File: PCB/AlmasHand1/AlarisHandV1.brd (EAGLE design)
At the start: 96.5 x 68.2 mm, 13 parts, among them M1 22-23-2021, M2 22-23-2021, M3 22-23-2021, M4 22-23-2021, M5 22-23-2021, M6 22-23-2021

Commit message: updates on board
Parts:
- moved U$1 2.54 mm to (25.4, 14.0)
- moved M1 2.54 mm to (10.2, 15.2)
- moved M2 2.54 mm to (10.2, 20.3)
- moved MOTOR_POWER_CONNECTOR 2.54 mm to (10.2, 27.9)
- moved UART 2.54 mm to (10.2, 38.1)
- moved U$2 1.27 mm to (66.0, 21.6)
- moved U$3 1.27 mm to (66.0, 48.3)
- moved M3 1.27 mm to (82.5, 47.0)
- moved M4 1.27 mm to (82.5, 41.9)
- moved M5 1.27 mm to (81.3, 20.3)
- moved M6 1.27 mm to (81.3, 15.2)
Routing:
- net 3.3V: track 0.00 -> 173.6 mm
- net GND: track 0.00 -> 137.1 mm
- net MOTOR_POWER: track 0.00 -> 114.9 mm
- net N$25: track 0.00 -> 60.5 mm
- net N$32: track 0.00 -> 54.6 mm
- net UART_RX: track 0.00 -> 54.6 mm
- net UART_TX: track 0.00 -> 53.7 mm
- net N$26: track 0.00 -> 48.9 mm
- net N$7: track 0.00 -> 45.2 mm
- net N$8: track 0.00 -> 37.9 mm
- net N$31: track 0.00 -> 36.4 mm
- net N$4: track 0.00 -> 21.7 mm
- net N$3: track 0.00 -> 21.5 mm
- net N$2: track 0.00 -> 15.1 mm
- net N$5: track 0.00 -> 12.0 mm
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
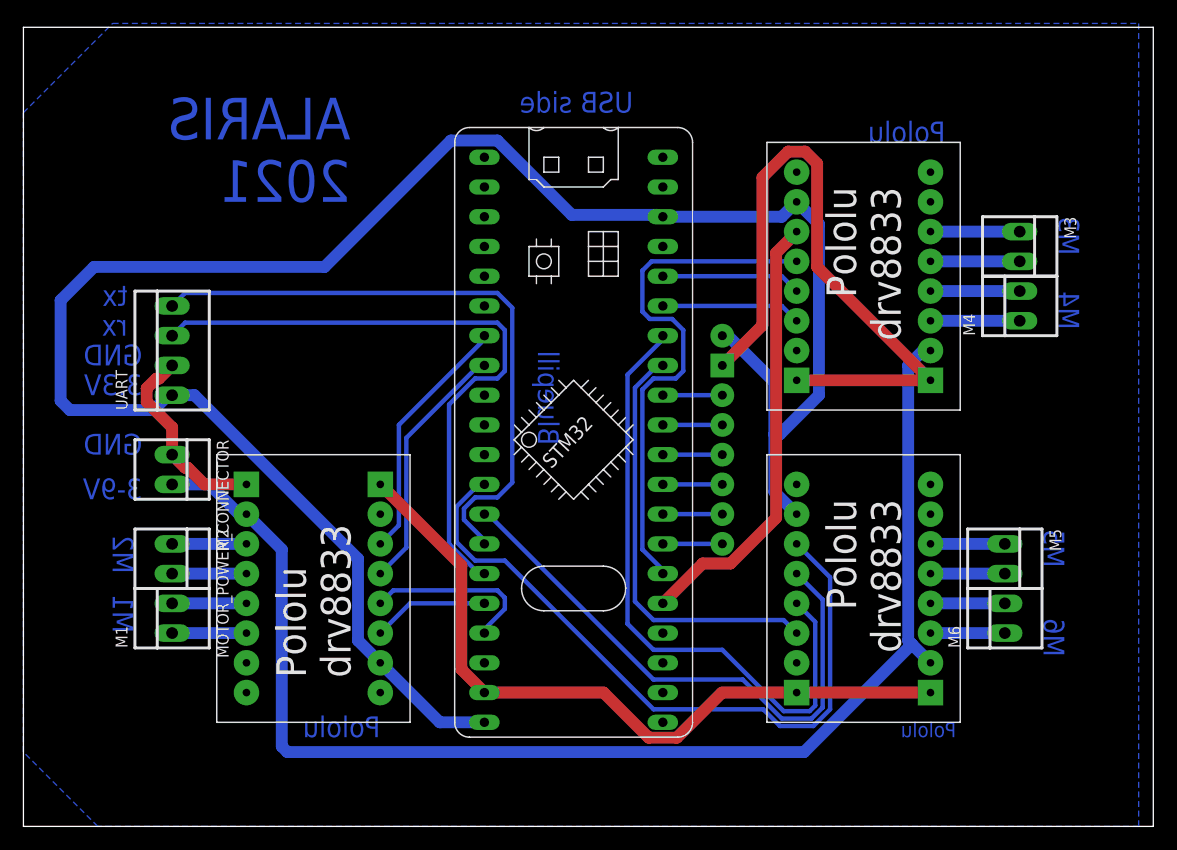
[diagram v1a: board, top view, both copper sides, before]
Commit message: Updated PCB drills for printing
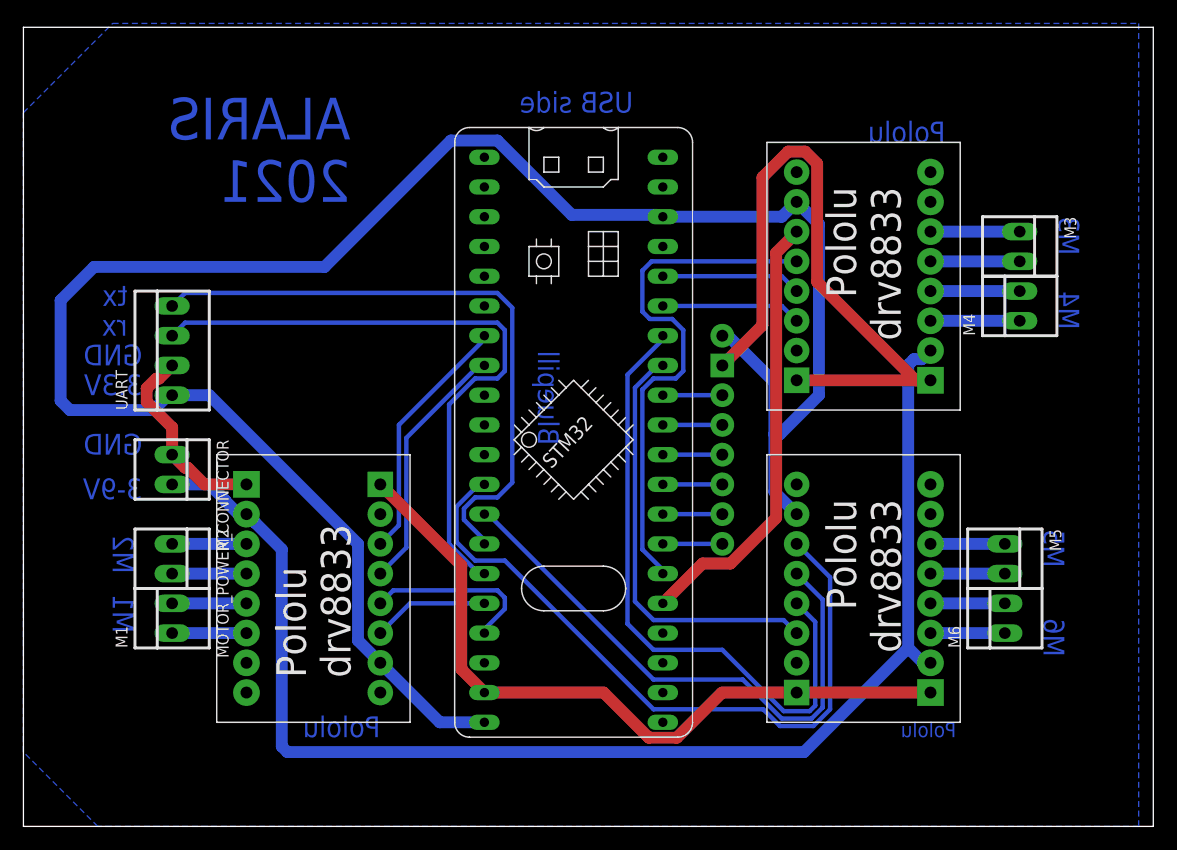
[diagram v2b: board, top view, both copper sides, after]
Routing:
- net GND: track 137.1 -> 137.9 mm
- net 3.3V: track 173.6 -> 174.3 mm
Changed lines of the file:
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@@
 <contactref element="MOTOR_POWER_CONNECTOR" pad="2"/>
 <wire x1="13.335" y1="26.67" x2="10.16" y2="26.67" width="1.016" layer="16"/>
-<wire x1="15.875" y1="24.13" x2="13.335" y2="26.67" width="1.016" layer="16"/>
-<wire x1="16.51" y1="24.13" x2="15.875" y2="24.13" width="1.016" layer="16"/>
-<wire x1="73.025" y1="13.335" x2="73.3425" y2="13.0175" width="1.016" layer="16"/>
-<wire x1="73.3425" y1="13.0175" x2="74.93" y2="11.43" width="1.016" layer="16"/>
-<wire x1="73.025" y1="36.83" x2="73.025" y2="13.335" width="1.016" layer="16"/>
-<wire x1="74.295" y1="38.1" x2="73.025" y2="36.83" width="1.016" layer="16"/>
-<wire x1="74.93" y1="38.1" x2="74.295" y2="38.1" width="1.016" layer="16"/>
-<wire x1="19.52625" y1="21.11375" x2="16.51" y2="24.13" width="1.016" layer="16"/>
-<wire x1="19.52625" y1="4.28625" x2="19.52625" y2="21.11375" width="1.016" layer="16"/>
 <wire x1="20.0025" y1="3.81" x2="19.52625" y2="4.28625" width="1.016" layer="16"/>
 <wire x1="64.135" y1="3.81" x2="20.0025" y2="3.81" width="1.016" layer="16"/>
-<wire x1="73.3425" y1="13.0175" x2="64.135" y2="3.81" width="1.016" layer="16"/>
+<wire x1="73.025" y1="12.7" x2="64.135" y2="3.81" width="1.016" layer="16"/>
+<wire x1="17.25699375" y1="23.3934" x2="17.2466" y2="23.3934" width="1.016" layer="16"/>
+<wire x1="17.2466" y1="23.3934" x2="16.51" y2="24.13" width="1.016" layer="16"/>
+<wire x1="19.52625" y1="4.28625" x2="19.52625" y2="21.12414375" width="1.016" layer="16"/>
+<wire x1="19.52625" y1="21.12414375" x2="17.25699375" y2="23.3934" width="1.016" layer="16"/>
+<wire x1="14.7066" y1="25.25345625" x2="14.7066" y2="25.2984" width="1.016" layer="16"/>
+<wire x1="14.7066" y1="25.2984" x2="13.335" y2="26.67" width="1.016" layer="16"/>
+<wire x1="16.51" y1="24.13" x2="15.83005625" y2="24.13" width="1.016" layer="16"/>
+<wire x1="15.83005625" y1="24.13" x2="14.7066" y2="25.25345625" width="1.016" layer="16"/>
+<wire x1="74.93" y1="38.1" x2="74.1934" y2="37.3634" width="1.016" layer="16"/>
+<wire x1="74.1934" y1="37.3634" x2="73.51345625" y2="37.3634" width="1.016" layer="16"/>
+<wire x1="73.51345625" y1="37.3634" x2="73.025" y2="36.87494375" width="1.016" layer="16"/>
+<wire x1="73.025" y1="36.87494375" x2="73.025" y2="12.7" width="1.016" layer="16"/>
+<wire x1="74.93" y1="11.43" x2="74.295" y2="11.43" width="1.016" layer="16"/>
+<wire x1="74.295" y1="11.43" x2="73.025" y2="12.7" width="1.016" layer="16"/>
 </signal>
 <signal name="N$16">
@@
 <wire x1="64.22595625" y1="55.0926" x2="62.77404375" y2="55.0926" width="1.016" layer="1"/>
 <wire x1="60.579" y1="40.259" x2="57.15" y2="36.83" width="1.016" layer="1"/>
-<wire x1="65.2526" y1="45.2374" x2="65.2526" y2="54.06595625" width="1.016" layer="1"/>
-<wire x1="74.93" y1="35.56" x2="65.2526" y2="45.2374" width="1.016" layer="1"/>
+<wire x1="65.2526" y1="43.9674" x2="65.2526" y2="54.06595625" width="1.016" layer="1"/>
+<wire x1="74.93" y1="35.56" x2="73.66" y2="35.56" width="1.016" layer="1"/>
+<wire x1="73.66" y1="35.56" x2="65.2526" y2="43.9674" width="1.016" layer="1"/>
 <wire x1="62.77404375" y1="55.0926" x2="60.579" y2="52.89755625" width="1.016" layer="1"/>
 <wire x1="60.579" y1="52.89755625" x2="60.579" y2="40.259" width="1.016" layer="1"/>
@@
 <wire x1="33.02" y1="6.35" x2="36.83" y2="6.35" width="1.016" layer="16"/>
 <wire x1="27.94" y1="11.43" x2="33.02" y2="6.35" width="1.016" layer="16"/>
-<wire x1="12.065" y1="34.29" x2="10.16" y2="34.29" width="1.016" layer="16"/>
-<wire x1="26.035" y1="20.32" x2="12.065" y2="34.29" width="1.016" layer="16"/>
-<wire x1="26.035" y1="13.335" x2="26.035" y2="20.32" width="1.016" layer="16"/>
+<wire x1="13.335" y1="34.29" x2="10.16" y2="34.29" width="1.016" layer="16"/>
+<wire x1="26.035" y1="21.59" x2="13.335" y2="34.29" width="1.016" layer="16"/>
+<wire x1="26.035" y1="13.335" x2="26.035" y2="21.59" width="1.016" layer="16"/>
 <wire x1="27.94" y1="11.43" x2="26.035" y2="13.335" width="1.016" layer="16"/>
 <wire x1="44.29125" y1="49.68875" x2="51.59375" y2="49.68875" width="1.016" layer="16"/>

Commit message: fixed M1 port connection
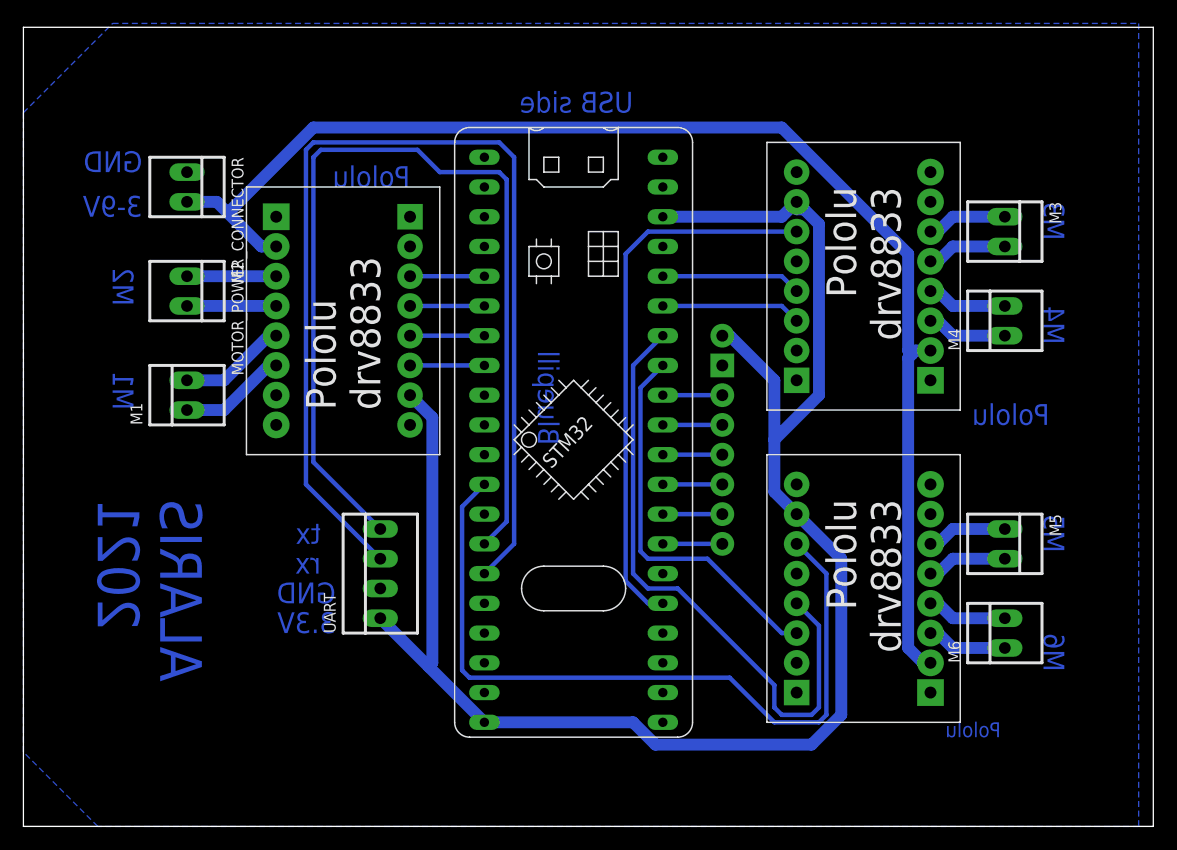
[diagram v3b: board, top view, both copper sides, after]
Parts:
- moved UART 26.1 mm to (27.9, 19.1)
- moved MOTOR_POWER_CONNECTOR 24.2 mm to (11.4, 52.1)
- moved U$1 23.0 mm to (27.9, 36.8)
- moved M2 22.9 mm to (11.4, 43.2)
- moved M1 19.1 mm to (11.4, 34.3)
- moved M3 1.80 mm to (81.3, 48.3)
- moved M4 1.80 mm to (81.3, 40.6)
- moved M5 1.27 mm to (81.3, 21.6)
- moved M6 1.27 mm to (81.3, 14.0)
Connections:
- net UART_TX renamed N$1
- removed net N$1 (its old number): U$1.INA1, U$4.P$16
- new net N$9: U$1.INB1, U$4.P$5
- net N$2: now also U$1.INA1, U$4.P$8; no longer U$1.INA2, U$4.P$17
- net N$3: now also U$1.INA2; no longer U$1.INB1
- net N$4: now also U$4.P$6; no longer U$4.P$8
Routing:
- net GND: track 137.9 -> 0.00 mm
- net N$26: track 48.9 -> 0.00 mm
- net N$7: track 45.2 -> 0.00 mm
- net UART_RX: track 54.6 -> 92.7 mm
- net 3.3V: track 174.3 -> 141.0 mm
- net N$1: track 53.7 -> 83.8 mm
- net N$4: track 21.7 -> 6.35 mm
- net N$3: track 21.5 -> 6.35 mm
- net N$1 (its old number): track 9.94 -> 0.00 mm
- net N$8: track 37.9 -> 47.3 mm
- net N$2: track 15.1 -> 6.35 mm
- net N$9: track 0.00 -> 6.35 mm
- net N$25: track 60.5 -> 65.5 mm
- net N$31: track 36.4 -> 32.9 mm
- net M1B: track 6.35 -> 9.20 mm
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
